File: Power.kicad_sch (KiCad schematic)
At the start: 51 parts, among them J31 USB_C_USB2.0_16P, J32 PinHeader_01x02_Pin, Q31 CSD16406Q3, Q32 CSD16406Q3, Q33 CSD25402Q3A, Q34 CSD25402Q3A, SW31 K3-1391B-51, U31 BH-18650-A6AJ012, U32 BQ29707, U33 MCP73833-FCI-MF, U34 INA260, U35 TPS61236PRWLR, U36 TPS63001DRCR

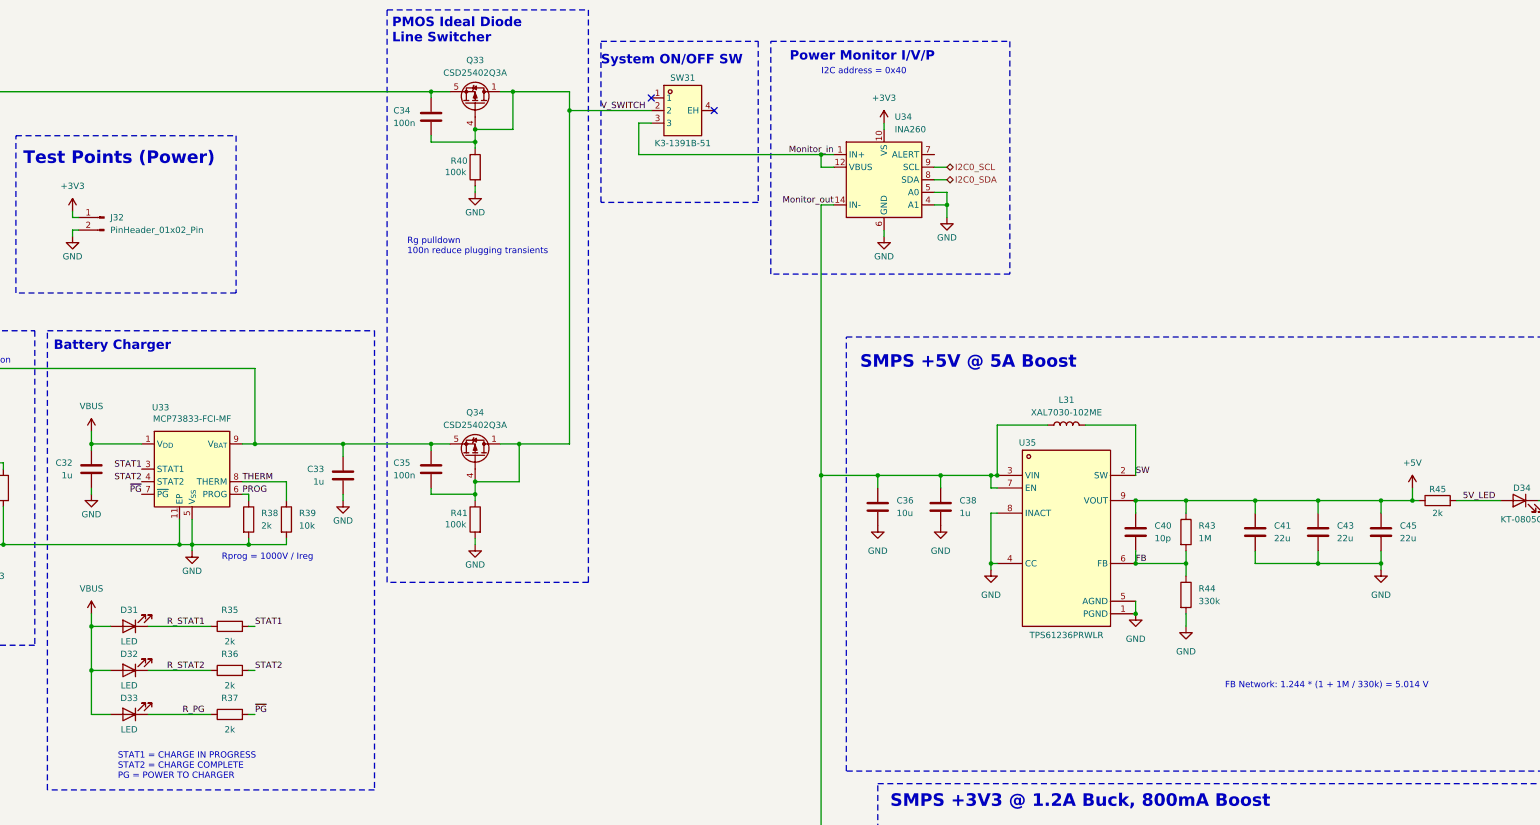
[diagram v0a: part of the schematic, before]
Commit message: Finish preliminary power layout
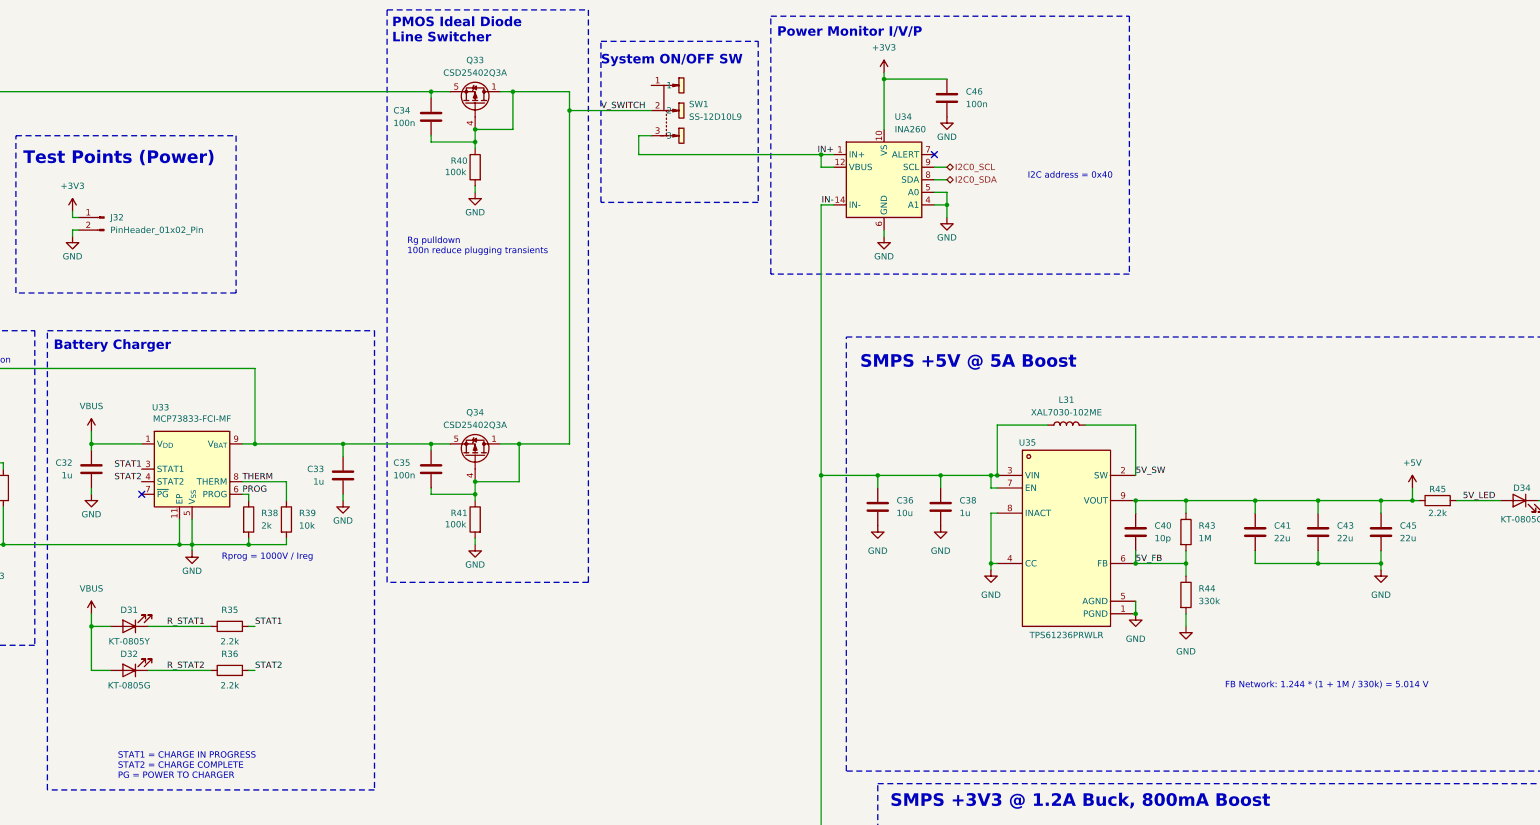
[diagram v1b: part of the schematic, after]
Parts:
- removed D33: LED, LED_SMD:LED_0805_2012Metric, symbol Device:LED
- removed R37: 2k, Resistor_SMD:R_0402_1005Metric, symbol Device:R
- removed SW31: K3-1391B-51, Slide_Switch:SW-TH_K3-1391B-51, symbol Slide_Switch:K3-1391B-51
- added C46: 100n, Capacitor_SMD:C_0402_1005Metric, symbol Device:C
- added SW1: SS-12D10L9, Slide_Switch:SW-TH_SS-12D10L9, symbol Slide_Switch:SS-12D10L9
- D31: value LED -> KT-0805Y
- D32: value LED -> KT-0805G
- R35, R36: value 2k -> 2.2k
- R45: value 2k -> 2.2k; footprint Resistor_SMD:R_0603_1608Metric -> Resistor_SMD:R_0402_1005Metric
- R46: footprint Resistor_SMD:R_0603_1608Metric -> Resistor_SMD:R_0402_1005Metric
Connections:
- net +3V3: now also C46.1
- net GND: now also C46.2
- net V_SWITCH: now also SW1.2
- net FB renamed 5V_FB
- net Monitor_in renamed IN+
- net IN+: now also SW1.3
- net Monitor_out renamed IN-
- net SW renamed 5V_SW
- net ~{PG}: no longer names the net of U33.7 (~{PG})

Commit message: v2 layouts done
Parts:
- C47: renamed from C31; value 0.1u -> 100n
- Q31, Q32: footprint Package_TO_SOT_SMD:TDSON-8-1 -> Package_SON:VSON-8_3.3x3.3mm_P0.65mm_NexFET
- R63: renamed from R44; footprint Resistor_SMD:R_0402_1005Metric -> Resistor_SMD:R_0603_1608Metric
- renumbered C32 to C48, C33 to C49, C34 to C50, C35 to C51, C36 to C52, C37 to C53, C38 to C54, C46 to C55, C39 to C56, C40 to C57, C41 to C58, C42 to C59, C43 to C60, C44 to C61, C45 to C62, D31 to D36, D32 to D37, D34 to D38, D35 to D39, J31 to J38, J32 to J39, L31 to L32, L32 to L33, R31 to R51, R32 to R52, R33 to R53, R34 to R54, R35 to R55, R36 to R56, R38 to R57, R39 to R58, R40 to R59, R41 to R60, R42 to R61, R43 to R62, R45 to R64, R46 to R65, SW1 to SW33, U31 to U33, U32 to U34, U33 to U35, U34 to U36, U35 to U37, U36 to U38
